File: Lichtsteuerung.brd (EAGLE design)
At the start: 157.7 x 86.4 mm, 173 parts, among them IC1 74HC595D, IC10 TSR_1-2450, IC11 MEGA64-A, IC12 75176AD, IC13 DS1307SO8, IC2 74HC595D, IC3 74HC595D, IC4 74HC595D, IC5 LM317LD, IC6 LM317LD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

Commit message: Updated part ordering numbers, added connector plugs and case to the BOM
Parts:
- C13, C19: value 220µ -> 10µ
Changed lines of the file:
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@@
 <setting verticaltext="up"/>
 </settings>
-<grid distance="1" unitdist="mm" unit="mm" style="lines" multiple="1" display="yes" altdistance="0.125" altunitdist="mm" altunit="mm"/>
+<grid distance="0.05" unitdist="inch" unit="inch" style="lines" multiple="1" display="yes" altdistance="0.025" altunitdist="inch" altunit="inch"/>
 <layers>
 <layer number="1" name="Top" color="4" fill="1" visible="yes" active="yes"/>
@@
 <attribute name="OC_NEWARK" value="92C6793" x="130.5" y="60" size="1.778" layer="27" rot="R90" display="off"/>
 <attribute name="NAME" x="127.98" y="62.917" size="0.6096" layer="25" align="center-left"/>
-<attribute name="OC_REICHELT" value="24FC128-I/SN" x="130.5" y="60" size="1.778" layer="27" rot="R90" display="off"/>
+<attribute name="OC_REICHELT" value="24FC1025-I/SM" x="130.5" y="60" size="1.778" layer="27" rot="R90" display="off"/>
 </element>
 <element name="IC10" library="_traco_tsr-1" package="TSR-1" value="TSR_1-2450" x="4" y="56" smashed="yes" rot="R270">
@@
 <element name="C11" library="rcl" package="C0805" value="22p" x="53.25" y="25.29" smashed="yes" rot="R270">
 <attribute name="NAME" x="54.73" y="23.5775" size="0.6096" layer="25" rot="R90" align="center-left"/>
-<attribute name="OC_REICHELT" value="X7R-G0805 22P" x="53.25" y="25.29" size="1.778" layer="27" rot="R270" display="off"/>
+<attribute name="OC_REICHELT" value="NPO-G0805 22P" x="53.25" y="25.29" size="1.778" layer="27" rot="R270" display="off"/>
 </element>
 <element name="C12" library="rcl" package="C0805" value="22p" x="44.79" y="25.77" smashed="yes" rot="R90">
 <attribute name="NAME" x="43.9925" y="28.2" size="0.6096" layer="25" align="center-left"/>
-<attribute name="OC_REICHELT" value="X7R-G0805 22P" x="44.79" y="25.77" size="1.778" layer="27" rot="R90" display="off"/>
+<attribute name="OC_REICHELT" value="NPO-G0805 22P" x="44.79" y="25.77" size="1.778" layer="27" rot="R90" display="off"/>
 </element>
 <element name="IC12" library="751xx" package="D_R-PDSO-G8" value="75176AD" x="45" y="60" smashed="yes" rot="R90">
@@
 <element name="IC11" library="avr-7" package="TQFP64" value="MEGA64-A" x="52.26" y="37.93" smashed="yes" rot="R315">
 <attribute name="NAME" x="57.755" y="45.135" size="0.6096" layer="25" rot="R315" align="center-left"/>
-<attribute name="OC_REICHELT" value="ATMEGA 64-16 TQ" x="52.26" y="37.93" size="1.778" layer="27" rot="R315" display="off"/>
+<attribute name="OC_REICHELT" value="ATMEGA 2561-16AU" x="52.26" y="37.93" size="1.778" layer="27" rot="R315" display="off"/>
 </element>
 <element name="R72" library="resistor" package="R0805" value="10k" x="54.8" y="52.11" smashed="yes">
@@
 <attribute name="OC_REICHELT" value="SMD-0805 10,0K" x="54.8" y="52.11" size="1.778" layer="27" display="off"/>
 </element>
-<element name="C13" library="rcl" package="C/6032-28R" value="220µ" x="20.3" y="48.63" smashed="yes">
+<element name="C13" library="rcl" package="C/6032-28R" value="10µ" x="20.3" y="48.63" smashed="yes">
 <attribute name="NAME" x="17.625" y="46.625" size="0.6096" layer="25" align="center-left"/>
-<attribute name="OC_REICHELT" value="VF 220/6,3 K-D" x="20.3" y="48.63" size="1.778" layer="27" display="off"/>
+<attribute name="PARTKEEPR_SKU" value="2607" x="20.3" y="48.63" size="1.778" layer="27" display="off"/>
 </element>
 <element name="C14" library="resistor" package="C0805" value="100n" x="41.5875" y="32.455" smashed="yes" rot="R225">
@@
 <element name="C15" library="resistor" package="A/3216-18R" value="1µ" x="108.5" y="48.75" smashed="yes" rot="R270">
 <attribute name="NAME" x="108.5" y="46.125" size="0.6096" layer="25" rot="R270" align="center-left"/>
-<attribute name="OC_REICHELT" value="VF 1,0/50 C-B" x="108.5" y="48.75" size="1.778" layer="27" rot="R270" display="off"/>
+<attribute name="PARTKEEPR_SKU" value="2609" x="108.5" y="48.75" size="1.778" layer="27" rot="R270" display="off"/>
 </element>
 <element name="C16" library="resistor" package="A/3216-18R" value="1µ" x="113.25" y="60.5" smashed="yes" rot="R270">
 <attribute name="NAME" x="113.99" y="63.52" size="0.6096" layer="25" rot="R180" align="center-left"/>
-<attribute name="OC_REICHELT" value="VF 1,0/50 C-B" x="113.25" y="60.5" size="1.778" layer="27" rot="R270" display="off"/>
+<attribute name="PARTKEEPR_SKU" value="2609" x="113.25" y="60.5" size="1.778" layer="27" rot="R270" display="off"/>
 </element>
 <element name="C17" library="resistor" package="A/3216-18R" value="1µ" x="106.25" y="48.75" smashed="yes" rot="R270">
 <attribute name="NAME" x="106.25" y="46" size="0.6096" layer="25" rot="R270" align="center-left"/>
-<attribute name="OC_REICHELT" value="VF 1,0/50 C-B" x="106.25" y="48.75" size="1.778" layer="27" rot="R270" display="off"/>
+<attribute name="PARTKEEPR_SKU" value="2609" x="106.25" y="48.75" size="1.778" layer="27" rot="R270" display="off"/>
 </element>
 <element name="C18" library="resistor" package="A/3216-18R" value="1µ" x="110.5" y="60.5" smashed="yes" rot="R90">
 <attribute name="NAME" x="109.795" y="63.27" size="0.6096" layer="25"/>
-<attribute name="OC_REICHELT" value="VF 1,0/50 C-B" x="110.5" y="60.5" size="1.778" layer="27" rot="R90" display="off"/>
+<attribute name="PARTKEEPR_SKU" value="2609" x="110.5" y="60.5" size="1.778" layer="27" rot="R90" display="off"/>
 </element>
 <element name="F1" library="f-lf-omniblok-s" package="OMNIBLOK" value="5V Rail 500mA" x="17" y="54" smashed="yes">
@@
 <attribute name="OC_REICHELT" value="SMD-0805 220" x="67.75" y="55.5" size="1.778" layer="27" rot="R90" display="off"/>
 </element>
-<element name="C19" library="rcl" package="C/6032-28R" value="220µ" x="87.78" y="59.34" smashed="yes" rot="R270">
-<attribute name="OC_REICHELT" value="VF 220/6,3 K-D" x="87.78" y="59.34" size="1.778" layer="27" rot="R270" display="off"/>
+<element name="C19" library="rcl" package="C/6032-28R" value="10µ" x="87.78" y="59.34" smashed="yes" rot="R270">
 <attribute name="NAME" x="87.115" y="63.845" size="0.6096" layer="25" align="center-left"/>
+<attribute name="PARTKEEPR_SKU" value="2607" x="87.78" y="59.34" size="1.778" layer="27" rot="R270" display="off"/>
 </element>
 <element name="C20" library="rcl" package="C0805" value="100n" x="39.375" y="61" smashed="yes" rot="R90">
@@
 <attribute name="OC_NEWARK" value="unknown" x="-110.81" y="-10.34" size="1.778" layer="27" display="off"/>
 <attribute name="NAME" x="148.79" y="38.18" size="0.6096" layer="25" ratio="10" rot="R180" align="center-left"/>
+<attribute name="OC_REICHELT" value="LTV 356T-SMD" x="147" y="43" size="1.778" layer="27" display="off"/>
 </element>
 <element name="R116" library="resistor" package="R0805" value="1.2k" x="147.87" y="25.86" smashed="yes" rot="R270">
@@
 <element name="X4" library="con-wago_2.5mm" package="P-733-332" value="733-332" x="112.25" y="7.375" smashed="yes" rot="R90">
 <attribute name="NAME" x="108.23" y="9.725" size="1.016" layer="25" font="vector" ratio="10" rot="R90"/>
+<attribute name="OC_REICHELT" value="WAGO 733-332" x="112.25" y="7.375" size="1.016" layer="27" rot="R90" display="off"/>
 </element>
 <element name="LED3" library="led" package="CHIP-LED0805" value="ACT" x="7.25" y="82" smashed="yes">
@@
 <element name="IC6" library="linear" package="SO08" value="LM317LD" x="67" y="30" smashed="yes">
 <attribute name="NAME" x="64.333" y="30.595" size="0.6096" layer="25" rot="R90"/>
+<attribute name="OC_REICHELT" value="LM 317 LD" x="67" y="30" size="1.778" layer="27" display="off"/>
 </element>
 <element name="R15" library="resistor" package="R0805" value="125" x="67.5" y="24.75" smashed="yes" rot="R180">
@@
 <element name="IC5" library="linear" package="SO08" value="LM317LD" x="101" y="38" smashed="yes">
 <attribute name="NAME" x="98.333" y="36.095" size="0.6096" layer="25" rot="R90"/>
+<attribute name="OC_REICHELT" value="LM 317 LD" x="101" y="38" size="1.778" layer="27" display="off"/>
 </element>
 <element name="R16" library="resistor" package="R0805" value="125" x="102.125" y="32.5" smashed="yes" rot="R180">
@@
 <element name="IC7" library="linear" package="SO08" value="LM317LD" x="153" y="52" smashed="yes">
 <attribute name="NAME" x="156.333" y="50.095" size="0.6096" layer="25" rot="R90"/>
+<attribute name="OC_REICHELT" value="LM 317 LD" x="153" y="52" size="1.778" layer="27" display="off"/>
 </element>
 <element name="R17" library="resistor" package="R0805" value="125" x="154.5" y="45" smashed="yes" rot="R270">
@@
 <element name="JP10" library="adafruit" package="1X10-BIG" value="PINHD-1X10" x="144" y="82" smashed="yes">
 <attribute name="NAME" x="131.3688" y="84.0788" size="1.016" layer="25" align="center-left"/>
+<attribute name="OC_REICHELT" value="BL 1X10G8 2,54" x="144" y="82" size="1.016" layer="27" display="off"/>
 </element>
 </elements>

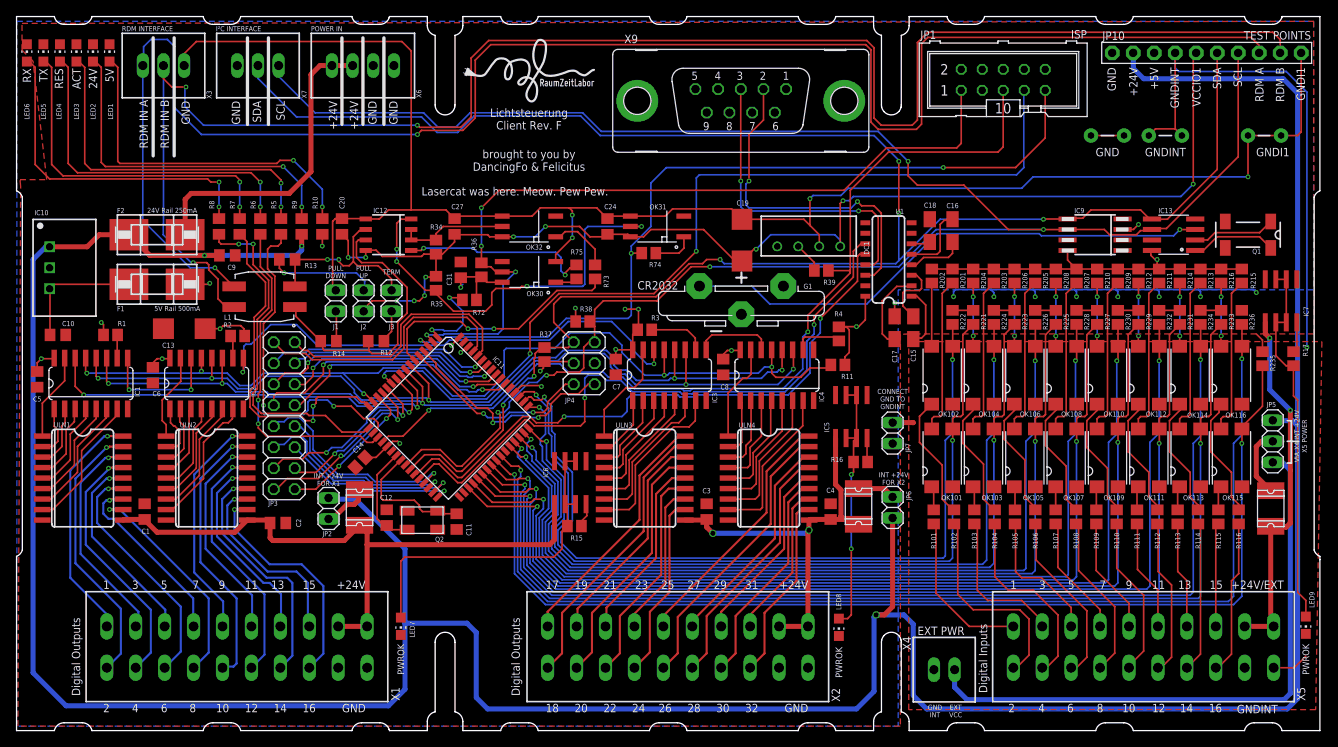
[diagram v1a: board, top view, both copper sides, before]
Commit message: Fixed LM317 to use constant current mode
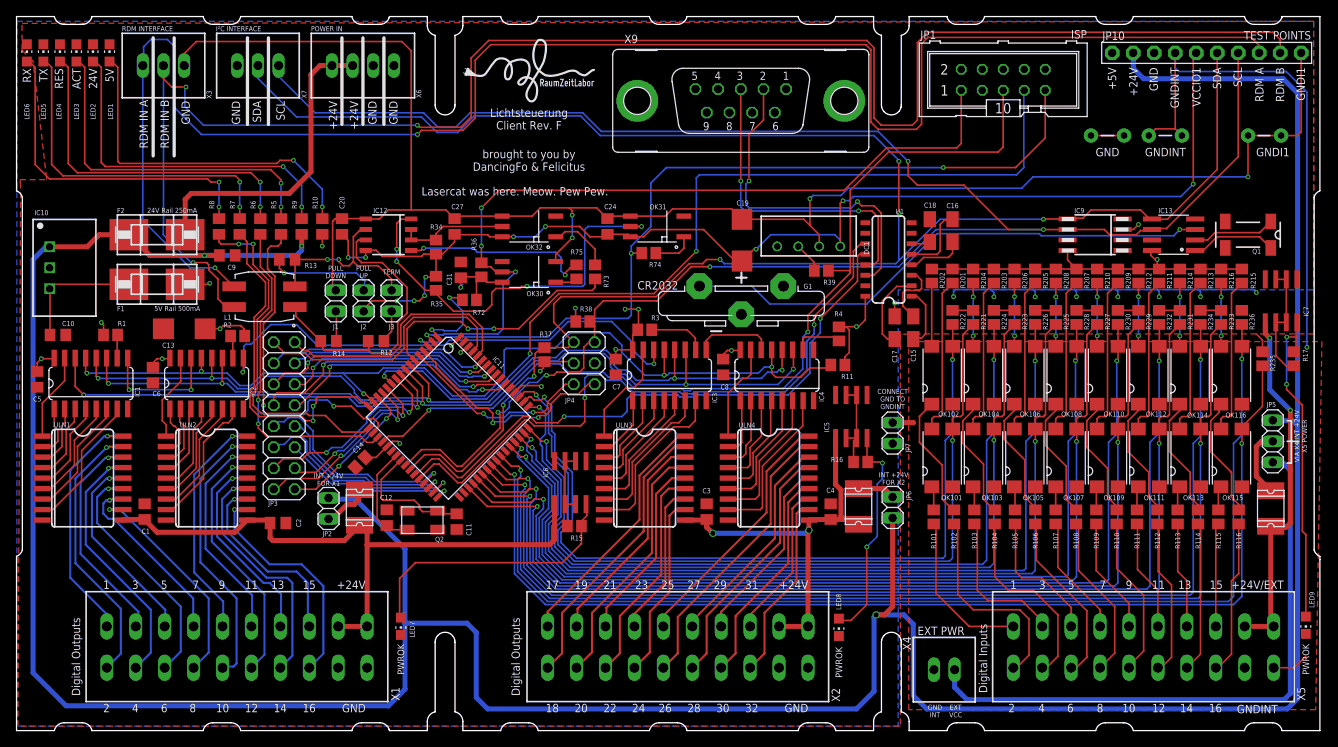
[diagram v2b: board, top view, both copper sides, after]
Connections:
- net N$80: now also LED8.A
- net N$82: no longer LED8.A
- net N$83: now also LED9.A
- net N$85: now also LED7.A
- net N$86: no longer LED7.A
- net N$88: no longer LED9.A
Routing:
- net N$83: track 3.72 -> 40.4 mm, vias 0 -> 2
- net N$88: track 45.4 -> 14.4 mm
- net N$85: track 2.96 -> 33.6 mm
- net N$86: track 40.5 -> 10.5 mm
- net N$80: track 2.93 -> 27.0 mm, vias 0 -> 2
- net N$82: track 31.1 -> 10.8 mm, vias 2 -> 0
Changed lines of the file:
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@@
 GND TO
 GNDINT</text>
-<text x="132.5" y="80.25" size="1.016" layer="25" rot="R270" align="center-left">GND</text>
+<text x="137.58" y="80.25" size="1.016" layer="25" rot="R270" align="center-left">GND</text>
 <text x="135.125" y="80.25" size="1.016" layer="25" rot="R270" align="center-left">+24V</text>
-<text x="137.625" y="80.25" size="1.016" layer="25" rot="R270" align="center-left">+5V</text>
+<text x="132.545" y="80.25" size="1.016" layer="25" rot="R270" align="center-left">+5V</text>
 <text x="140.125" y="80.25" size="1.016" layer="25" rot="R270" align="center-left">GNDINT</text>
 <text x="142.75" y="80.25" size="1.016" layer="25" rot="R270" align="center-left">VCCIO1</text>
@@
 </element>
 <element name="R17" library="resistor" package="R0805" value="125" x="154.5" y="45" smashed="yes" rot="R270">
-<attribute name="NAME" x="155.641" y="46.762" size="0.6096" layer="25" rot="R270"/>
+<attribute name="NAME" x="155.641" y="46.127" size="0.6096" layer="25" rot="R270"/>
 </element>
 <element name="LED9" library="led" package="CHIP-LED0805" value="PWROK" x="156" y="12.75" smashed="yes" rot="R180">
@@
 <wire x1="69" y1="26" x2="69" y2="27.305" width="0.2032" layer="1"/>
 <wire x1="69" y1="27.305" x2="68.905" y2="27.4" width="0.2032" layer="1"/>
+<contactref element="LED7" pad="A"/>
+<wire x1="68.35" y1="24.75" x2="68.35" y2="22.63" width="0.2032" layer="1"/>
+<wire x1="68.35" y1="22.63" x2="66.04" y2="20.32" width="0.2032" layer="1"/>
+<wire x1="66.04" y1="20.32" x2="48.26" y2="20.32" width="0.2032" layer="1"/>
+<wire x1="48.26" y1="20.32" x2="46.355" y2="18.415" width="0.2032" layer="1"/>
+<wire x1="46.355" y1="18.415" x2="46.355" y2="13.82" width="0.2032" layer="1"/>
+<wire x1="46.355" y1="13.82" x2="46.5" y2="13.675" width="0.2032" layer="1"/>
 </signal>
 <signal name="N$86">
@@
 <contactref element="IC6" pad="6"/>
 <contactref element="IC6" pad="3"/>
-<contactref element="LED7" pad="A"/>
-<wire x1="46.5" y1="13.675" x2="46.5" y2="20.5" width="0.2032" layer="1"/>
-<wire x1="46.5" y1="20.5" x2="47" y2="21" width="0.2032" layer="1"/>
-<wire x1="47" y1="21" x2="65" y2="21" width="0.2032" layer="1"/>
-<wire x1="65" y1="21" x2="66" y2="22" width="0.2032" layer="1"/>
-<wire x1="66" y1="22" x2="66" y2="24.1" width="0.2032" layer="1"/>
-<wire x1="66" y1="24.1" x2="66.65" y2="24.75" width="0.2032" layer="1"/>
 <wire x1="66.65" y1="24.75" x2="66.65" y2="27.115" width="0.2032" layer="1"/>
 <wire x1="66.65" y1="27.115" x2="66.365" y2="27.4" width="0.2032" layer="1"/>
@@
 <wire x1="102.905" y1="35.4" x2="102.905" y2="32.57" width="0.2032" layer="1"/>
 <wire x1="102.905" y1="32.57" x2="102.975" y2="32.5" width="0.2032" layer="1"/>
+<contactref element="LED8" pad="A"/>
+<wire x1="102.975" y1="32.5" x2="104.66" y2="32.5" width="0.2032" layer="1"/>
+<wire x1="104.66" y1="32.5" x2="104.775" y2="32.385" width="0.2032" layer="1"/>
+<via x="104.775" y="32.385" extent="1-16" drill="0.3"/>
+<wire x1="104.775" y1="32.385" x2="104.775" y2="30.48" width="0.2032" layer="16"/>
+<wire x1="104.775" y1="30.48" x2="104.14" y2="29.845" width="0.2032" layer="16"/>
+<wire x1="104.14" y1="29.845" x2="104.14" y2="23.495" width="0.2032" layer="16"/>
+<wire x1="104.14" y1="23.495" x2="102.87" y2="22.225" width="0.2032" layer="16"/>
+<via x="102.87" y="22.225" extent="1-16" drill="0.3"/>
+<wire x1="102.87" y1="22.225" x2="102.87" y2="15.24" width="0.2032" layer="1"/>
+<wire x1="102.87" y1="15.24" x2="100.965" y2="13.335" width="0.2032" layer="1"/>
+<wire x1="100.965" y1="13.335" x2="99.715" y2="13.335" width="0.2032" layer="1"/>
+<wire x1="99.715" y1="13.335" x2="99.5" y2="13.55" width="0.2032" layer="1"/>
 </signal>
 <signal name="N$82">
@@
 <contactref element="IC5" pad="6"/>
 <contactref element="IC5" pad="3"/>
-<contactref element="LED8" pad="A"/>
 <wire x1="100.365" y1="40.6" x2="101.635" y2="40.6" width="0.2032" layer="1"/>
 <wire x1="100.365" y1="35.4" x2="101.635" y2="35.4" width="0.2032" layer="1"/>
@@
 <wire x1="101.275" y1="32.5" x2="101.275" y2="35.04" width="0.2032" layer="1"/>
 <wire x1="101.275" y1="35.04" x2="101.635" y2="35.4" width="0.2032" layer="1"/>
-<wire x1="101.275" y1="32.5" x2="101.275" y2="31.275" width="0.2032" layer="1"/>
-<wire x1="101.275" y1="31.275" x2="101" y2="31" width="0.2032" layer="1"/>
-<via x="101" y="31" extent="1-16" drill="0.3"/>
-<wire x1="101" y1="31" x2="101" y2="22" width="0.2032" layer="16"/>
-<via x="101" y="22" extent="1-16" drill="0.3"/>
-<wire x1="99.5" y1="13.55" x2="100.55" y2="13.55" width="0.2032" layer="1"/>
-<wire x1="100.55" y1="13.55" x2="101" y2="14" width="0.2032" layer="1"/>
-<wire x1="101" y1="14" x2="101" y2="22" width="0.2032" layer="1"/>
 </signal>
 <signal name="N$83">
 <contactref element="IC7" pad="4"/>
 <contactref element="R17" pad="1"/>
-<wire x1="154.905" y1="49.4" x2="154.905" y2="46.255" width="0.2032" layer="1"/>
+<wire x1="154.94" y1="49.365" x2="154.94" y2="47.625" width="0.2032" layer="1"/>
 <wire x1="154.905" y1="46.255" x2="154.5" y2="45.85" width="0.2032" layer="1"/>
+<contactref element="LED9" pad="A"/>
+<wire x1="156" y1="13.8" x2="156" y2="23.705" width="0.2032" layer="1"/>
+<wire x1="156" y1="23.705" x2="155.575" y2="24.13" width="0.2032" layer="1"/>
+<wire x1="154.94" y1="46.29" x2="154.94" y2="47.625" width="0.2032" layer="1"/>
+<wire x1="154.94" y1="47.625" x2="153.67" y2="47.625" width="0.2032" layer="1"/>
+<via x="153.67" y="47.625" extent="1-16" drill="0.3"/>
+<wire x1="153.67" y1="47.625" x2="153.67" y2="41.91" width="0.2032" layer="16"/>
+<via x="153.67" y="41.91" extent="1-16" drill="0.3"/>
+<wire x1="153.67" y1="41.91" x2="153.67" y2="41.275" width="0.2032" layer="1"/>
+<wire x1="153.67" y1="41.275" x2="155.575" y2="39.37" width="0.2032" layer="1"/>
+<wire x1="155.575" y1="39.37" x2="155.575" y2="24.13" width="0.2032" layer="1"/>
+<wire x1="154.94" y1="49.365" x2="154.905" y2="49.4" width="0.2032" layer="1"/>
+<wire x1="154.94" y1="46.29" x2="154.5" y2="45.85" width="0.2032" layer="1"/>
 </signal>
 <signal name="N$88">
@@
 <contactref element="IC7" pad="6"/>
 <contactref element="IC7" pad="3"/>
-<contactref element="LED9" pad="A"/>
 <wire x1="152.365" y1="49.4" x2="153.635" y2="49.4" width="0.2032" layer="1"/>
 <wire x1="153.635" y1="49.4" x2="153.635" y2="54.6" width="0.2032" layer="1"/>
@@
 <wire x1="152.375" y1="45.375" x2="152.375" y2="49.39" width="0.2032" layer="1"/>
 <wire x1="152.375" y1="49.39" x2="152.365" y2="49.4" width="0.2032" layer="1"/>
-<wire x1="156" y1="13.8" x2="156" y2="15.75" width="0.2032" layer="1"/>
-<wire x1="155" y1="16.75" x2="155" y2="40" width="0.2032" layer="1"/>
-<wire x1="155" y1="40" x2="154.5" y2="40.5" width="0.2032" layer="1"/>
-<wire x1="154.5" y1="40.5" x2="154.5" y2="44.15" width="0.2032" layer="1"/>
-<wire x1="155" y1="16.75" x2="156" y2="15.75" width="0.2032" layer="1"/>
 </signal>
 </signals>
